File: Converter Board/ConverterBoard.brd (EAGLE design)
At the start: 101.6 x 101.3 mm, 43 parts

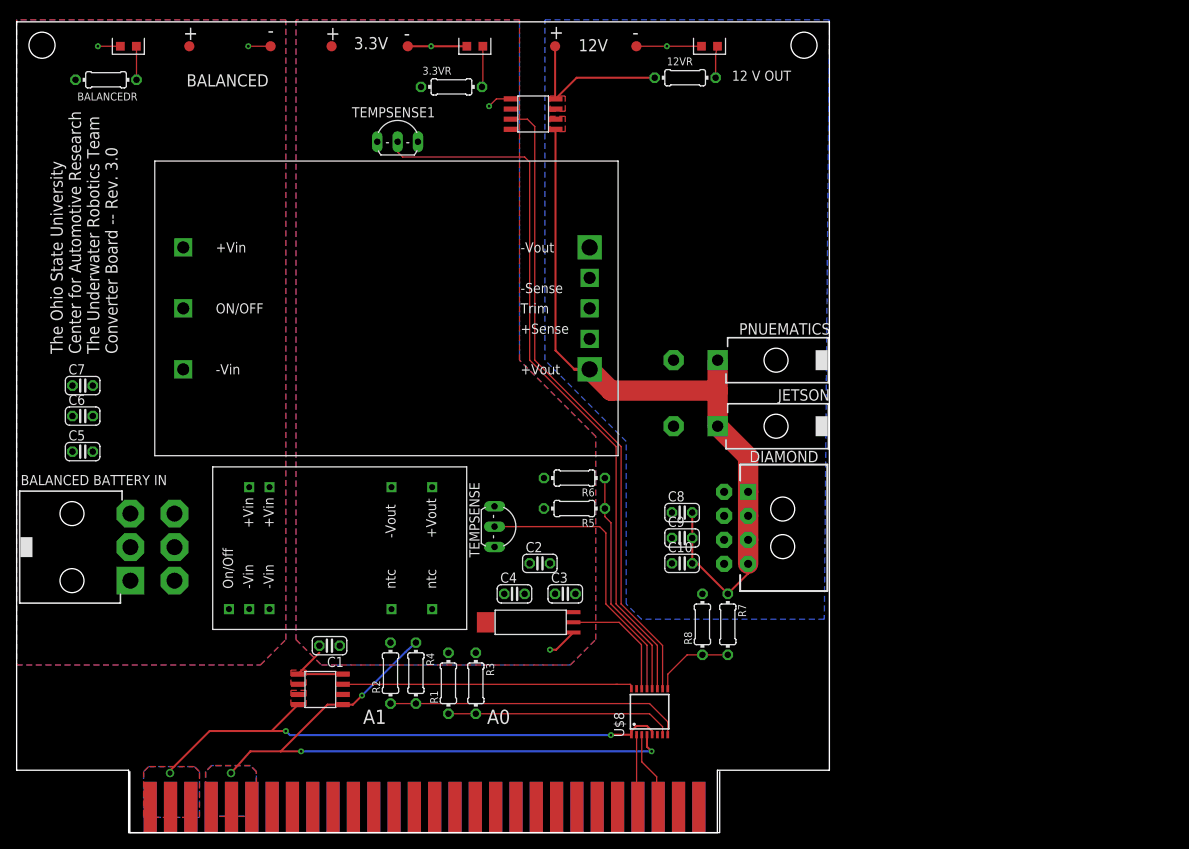
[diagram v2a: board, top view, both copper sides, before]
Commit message: Added correct capacitors, rearranged parts
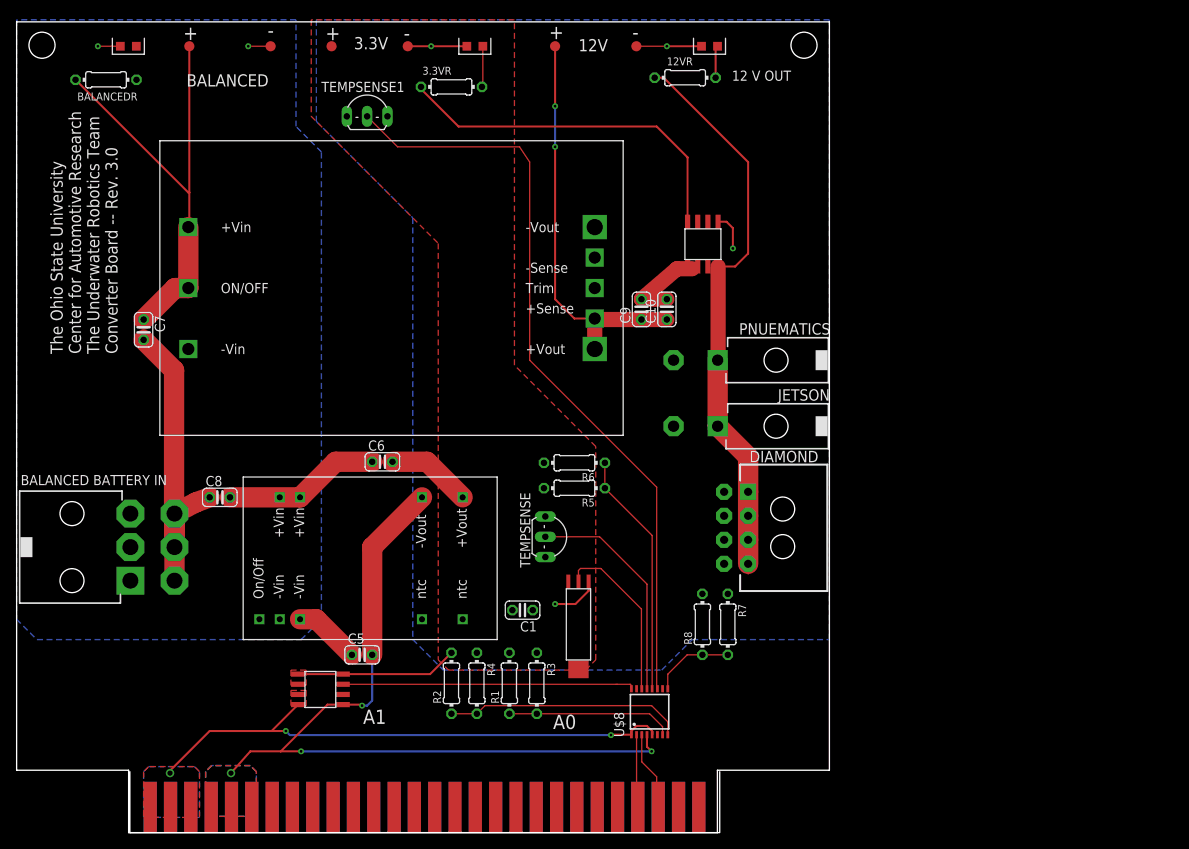
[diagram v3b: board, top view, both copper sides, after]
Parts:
- removed C2, C3, C4: (no value), resistor:C025-024X044
- C10, C8: value (none) -> 1uF
- C5, C6: value (none) -> 1000pF
- C7: value (none) -> 220uF
- C9: value (none) -> 10uF
- moved C8 57.8 mm to (25.4, 41.9)
- moved C5 43.2 mm to (43.2, 22.2)
- moved C6 37.9 mm to (45.7, 46.4)
- moved C10 31.8 mm to (81.3, 65.4), turned to 90 degrees
- moved C9 29.0 mm to (78.1, 65.4), turned to 90 degrees
- moved C1 24.5 mm to (63.2, 27.8)
- moved 12VCURRENT 23.8 mm to (83.9, 70.8), turned to 0 degrees
- moved C7 10.3 mm to (15.9, 62.9), turned to 270 degrees
- moved R2 7.73 mm to (54.4, 18.7)
- moved R4 7.73 mm to (57.5, 18.7)
- moved R1 7.62 mm to (61.6, 18.7)
- moved R3 7.62 mm to (65.0, 18.7)
- moved U$6 6.63 mm to (71.5, 31.4), turned to 180 degrees
- moved TEMPSENSE 6.48 mm to (66.1, 37.0)
- moved TEMPSENSE1 4.96 mm to (43.8, 89.5)
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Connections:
- removed net 12VGND: 12V-TP.TP, 12VCONVERTER.4,-VOUT, 12VLED.CATHODE, C10.1, C8.1, C9.1, DIAMOND.5, DIAMOND.6, DIAMOND.7, DIAMOND.8, JETSON.2, PNUEMATICS.2, R8.2
- removed net 12VMON: 12V+TP.TP, 12VCURRENT.3,IP-, 12VCURRENT.4,IP-, 12VR.1
- removed net 12VUNMON: 12VCONVERTER.8,+VOUT, 12VCURRENT.1,IP+, 12VCURRENT.2,IP+, C10.2, C8.2, C9.2, DIAMOND.1, DIAMOND.2, DIAMOND.3, DIAMOND.4, JETSON.1, PNUEMATICS.1, R7.1
- new net 12V+: 12V+TP.TP, 12VCONVERTER.7,+SENSE, 12VCONVERTER.8,+VOUT, C10.1, C9.1
- new net 12VCIN: 12VCONVERTER.1,+VIN, 12VCONVERTER.2,ON/OFF, 12VCURRENT.1,IP+, 12VCURRENT.2,IP+, BALANCED+TP.TP, BALANCEDR.2, C10.2, C7.1, C9.2, R7.1
- new net 12VCOUT: 12VCURRENT.3,IP-, 12VCURRENT.4,IP-, 12VR.1, DIAMOND.1, DIAMOND.2, DIAMOND.3, DIAMOND.4, JETSON.1, PNUEMATICS.1
- new net 3.3VC: C6.1, C8.2, U$2.22, U$2.23
- new net GND: 12V-TP.TP, 12VCONVERTER.4,-VOUT, 12VCONVERTER.5,-SENSE, 12VCURRENT.5,GND, 12VLED.CATHODE, 3.3V-TP.TP, 3.3VCURRENT.5,GND, 3.3VLED.CATHODE, C1.1, C5.2, DIAMOND.5, DIAMOND.6, DIAMOND.7, DIAMOND.8, JETSON.2, PNUEMATICS.2, R3.1, R4.1, R5.2, R8.2, TEMPSENSE.B, TEMPSENSE1.B, U$2.16, U$6.-VE, U$8.GND
- net 3.3V+: now also C6.2; no longer C2.2, C3.2, C4.2
- net 3.3VGND: no longer 12VCURRENT.5,GND, 3.3V-TP.TP, 3.3VCURRENT.5,GND, 3.3VLED.CATHODE, C1.1, C2.1, C3.1, C4.1, R3.1, R4.1, R5.2, TEMPSENSE.B, TEMPSENSE1.B, U$2.16, U$6.-VE, U$8.GND
- net BALANCED+: now also C8.1; no longer 12VCONVERTER.1,+VIN, 12VCONVERTER.2,ON/OFF, BALANCED+TP.TP, BALANCEDR.2, C5.2, C6.2, U$2.22, U$2.23
- net BALANCEDGND: no longer C6.1, C7.1
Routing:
- net GND: track 0.00 -> 125.0 mm, vias 0 -> 8
- net 12VUNMON: track 94.2 -> 0.00 mm
- net 3.3VGND: track 93.4 -> 0.00 mm, vias 7 -> 0
- net 12IDATA: track 80.3 -> 0.00 mm
- net 12VCOUT: track 0.00 -> 72.0 mm
- net 12VCIN: track 0.00 -> 68.5 mm
- net 3.3V+: track 9.37 -> 76.1 mm
- net 12V+: track 0.00 -> 50.5 mm, vias 0 -> 2
- net BALANCED+: track 0.00 -> 40.7 mm
- net 12VMON: track 20.1 -> 0.00 mm
- net 3.3VC: track 0.00 -> 19.6 mm
- net BALANCEDGND: track 5.60 -> 13.9 mm
- net 12VGND: track 8.14 -> 0.00 mm, vias 1 -> 0
- net TEMPDATA: track 35.8 -> 28.2 mm
- net A0: track 28.4 -> 20.8 mm
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- added copper zone on layer 16, net GND
- removed copper zone on layer 16, net 12VGND
- removed copper zone on layer 1, net 12VMON
- removed copper zone on layer 1, net 12VUNMON
- removed copper zone on layer 1, net BALANCED+

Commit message: Finished Rev 3 of converter board
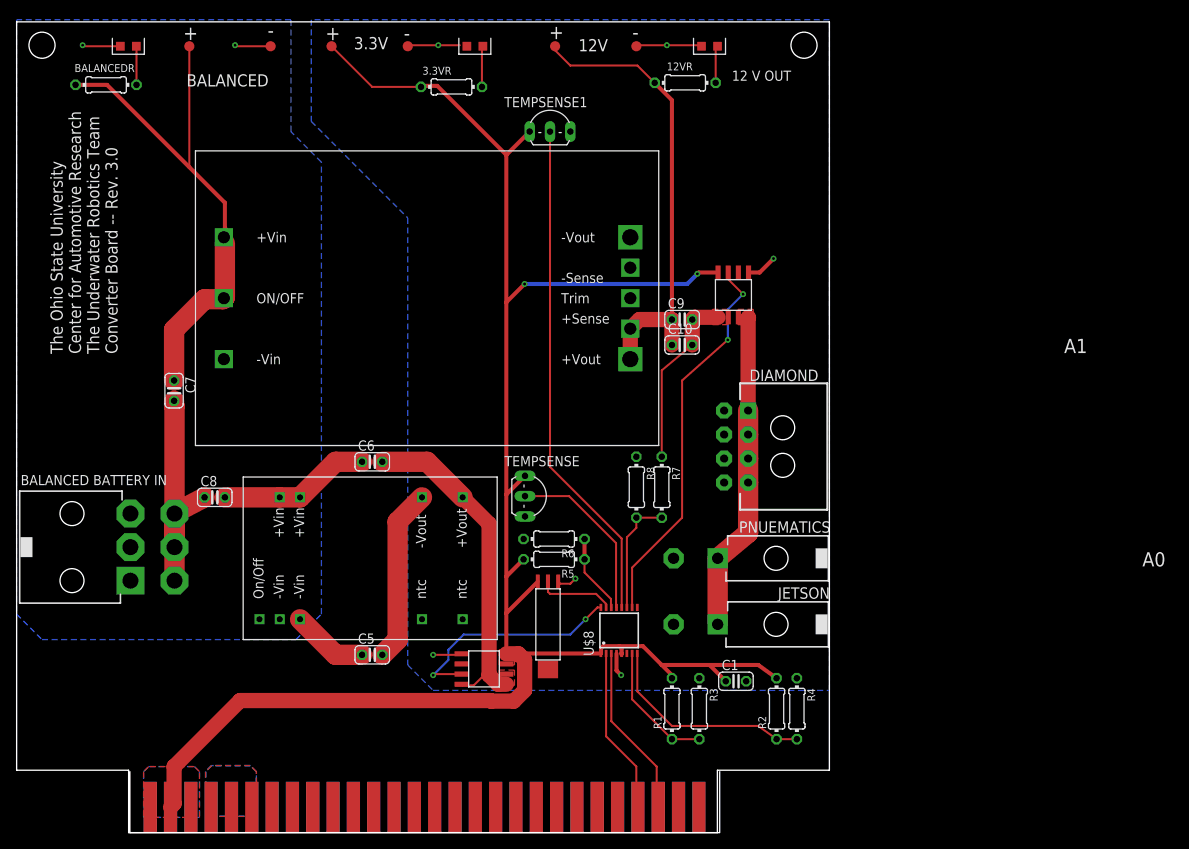
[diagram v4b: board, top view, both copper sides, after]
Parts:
- moved R2 40.8 mm to (95.0, 15.5)
- moved R4 40.1 mm to (97.5, 15.5)
- moved C1 28.1 mm to (89.9, 18.9), turned to 0 degrees
- moved 3.3VCURRENT 26.1 mm to (61.2, 18.5), turned to 90 degrees
- moved PNUEMATICS 24.8 mm to (87.6, 34.3)
- moved JETSON 24.8 mm to (87.6, 26.0)
- moved TEMPSENSE1 22.9 mm to (66.7, 87.6)
- moved R1 20.6 mm to (81.9, 15.5)
- moved R3 20.6 mm to (85.3, 15.5)
- moved R7 19.0 mm to (80.6, 43.2)
- moved R8 19.0 mm to (77.5, 43.2), turned to 270 degrees
- moved U$8 10.9 mm to (75.3, 25.3)
- moved DIAMOND 10.2 mm to (91.4, 48.3)
- moved R6 9.86 mm to (67.2, 36.7)
- moved R5 9.25 mm to (67.2, 34.2)
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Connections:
- net 12IDATA renamed 12VCURRENTDATA
- net 3.3IDATA renamed 3.3VCURRENTDATA
- net 3.3VC renamed 3.3VCONVIN
- removed net 12V+: 12V+TP.TP, 12VCONVERTER.7,+SENSE, 12VCONVERTER.8,+VOUT, C10.1, C9.1
- removed net 12VCIN: 12VCONVERTER.1,+VIN, 12VCONVERTER.2,ON/OFF, 12VCURRENT.1,IP+, 12VCURRENT.2,IP+, BALANCED+TP.TP, BALANCEDR.2, C10.2, C7.1, C9.2, R7.1
- removed net 12VCOUT: 12VCURRENT.3,IP-, 12VCURRENT.4,IP-, 12VR.1, DIAMOND.1, DIAMOND.2, DIAMOND.3, DIAMOND.4, JETSON.1, PNUEMATICS.1
- removed net 12VDATA: R7.2, R8.1, U$8.IN7
- removed net 3.3V+: 12VCURRENT.8,VCC, 3.3V+TP.TP, 3.3VCURRENT.1,IP+, 3.3VCURRENT.2,IP+, 3.3VCURRENT.8,VCC, 3.3VR.2, C1.2, C6.2, R1.2, R2.2, R6.2, TEMPSENSE.E, TEMPSENSE1.E, U$2.14, U$6.+VE
- removed net GND: 12V-TP.TP, 12VCONVERTER.4,-VOUT, 12VCONVERTER.5,-SENSE, 12VCURRENT.5,GND, 12VLED.CATHODE, 3.3V-TP.TP, 3.3VCURRENT.5,GND, 3.3VLED.CATHODE, C1.1, C5.2, DIAMOND.5, DIAMOND.6, DIAMOND.7, DIAMOND.8, JETSON.2, PNUEMATICS.2, R3.1, R4.1, R5.2, R8.2, TEMPSENSE.B, TEMPSENSE1.B, U$2.16, U$6.-VE, U$8.GND
- removed net VCC: 3.3VCURRENT.3,IP-, 3.3VCURRENT.4,IP-, U$3.3.3VP1, U$3.3.3VP2, U$3.3.3VP3, U$3.3.3V_4, U$3.3.3V_5, U$3.3.3V_6, U$8.V+, U$8.VREF
- new net 12VCONV+: 12V+TP.TP, 12VCONVERTER.7,+SENSE, 12VCONVERTER.8,+VOUT, 12VR.1, C10.1, C9.1
- new net 12VCONVIN: 12VCONVERTER.1,+VIN, 12VCONVERTER.2,ON/OFF, BALANCED+TP.TP, BALANCEDR.1, C7.1
- new net 12VCURRENTIN: 12VCURRENT.1,IP+, 12VCURRENT.2,IP+, C10.2, C9.2, R7.1
- new net 12VCURRENTOUT: 12VCURRENT.3,IP-, 12VCURRENT.4,IP-, DIAMOND.1, DIAMOND.2, DIAMOND.3, DIAMOND.4, JETSON.1, PNUEMATICS.1
- new net 12VDIV: R7.2, R8.2, U$8.IN5
- new net 3.3VCONVOUT: 3.3VCURRENT.1,IP+, 3.3VCURRENT.2,IP+, 3.3VCURRENT.8,VCC, C6.2, U$2.14
- new net 3.3VCURRENTOUT: 12VCURRENT.8,VCC, 3.3V+TP.TP, 3.3VCURRENT.3,IP-, 3.3VCURRENT.4,IP-, 3.3VR.2, C1.1, R1.2, R2.2, R5.2, TEMPSENSE.E, TEMPSENSE1.E, U$3.3.3VP1, U$3.3.3VP2, U$3.3.3VP3, U$3.3.3V_4, U$3.3.3V_5, U$3.3.3V_6, U$6.+VE, U$8.V+, U$8.VREF
- new net CMGND: 12V-TP.TP, 12VCONVERTER.4,-VOUT, 12VCONVERTER.5,-SENSE, 12VCURRENT.5,GND, 12VLED.CATHODE, 3.3V-TP.TP, 3.3VCURRENT.5,GND, 3.3VLED.CATHODE, C1.2, C5.2, DIAMOND.5, DIAMOND.6, DIAMOND.7, DIAMOND.8, JETSON.2, PNUEMATICS.2, R3.1, R4.1, R6.2, R8.1, TEMPSENSE.B, TEMPSENSE1.B, U$2.16, U$6.-VE, U$8.GND
- net 3.3VDATA: now also U$8.IN2; no longer U$8.IN4
- net BALANCEDGND: no longer U$2.1
- net BALANCEDLED: now also BALANCEDR.2; no longer BALANCEDR.1
- net HUMIDITYDATA: now also U$8.IN1; no longer U$8.IN2
- net TEMP1DATA: now also U$8.IN4; no longer U$8.IN5
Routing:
- net 3.3VCURRENTOUT: track 0.00 -> 234.0 mm, vias 0 -> 2
- net GND: track 125.0 -> 0.00 mm, vias 8 -> 0
- net 3.3V+: track 76.1 -> 0.00 mm
- net 12VCOUT: track 72.0 -> 0.00 mm
- net VCC: track 69.0 -> 0.00 mm, vias 3 -> 0
- net 12VCIN: track 68.5 -> 0.00 mm
- net 12VCONVIN: track 0.00 -> 66.0 mm
- net 12VCONV+: track 0.00 -> 57.8 mm
- net CMGND: track 0.00 -> 51.2 mm, vias 0 -> 6
- net 12V+: track 50.5 -> 0.00 mm, vias 2 -> 0
- net 12VCURRENTDATA: track 0.00 -> 48.6 mm, vias 0 -> 2
- net 3.3VCONVOUT: track 0.00 -> 42.1 mm
- net 12VCURRENTOUT: track 0.00 -> 40.2 mm
- net TEMP1DATA: track 95.4 -> 63.2 mm
- net 12VCURRENTIN: track 0.00 -> 22.3 mm
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- added copper zone on layer 1, net 12VCURRENTIN
- added copper zone on layer 1, net 12VCURRENTOUT
- added copper zone on layer 1, net 3.3VCONVOUT
- added copper zone on layer 1, net 3.3VCURRENTOUT
- added copper zone on layer 16, net CMGND
- removed copper zone on layer 1, net 3.3V+
- removed copper zone on layer 1, net 3.3VBKPLN
- removed copper zone on layer 16, net GND

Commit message: Finished rev3 of board, made gerber files
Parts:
- removed C1: 0.1 uF, resistor:C025-024X044
- removed C10, C8: 1uF, resistor:C025-024X044
- removed C6: 1000pF, resistor:C025-024X044
- removed C7: 220uF, resistor:C025-024X044
- removed C9: 10uF, resistor:C025-024X044
- added C11, C14: 1uF, capacitor-wima:C5B3
- added C12: 220uF, capacitor-wima:C5B3
- added C13: 10uF, capacitor-wima:C5B3
- added C3, C4: 1000pF, capacitor-wima:C5B3
- added SCL, SDA: TPPAD1-20, testpad:P1-20
- C5: value 1000pF -> 0.1uF; device resistor:C025-024X044 -> capacitor-wima:C2.5-2
- moved C5 46.5 mm to (90.8, 19.1), turned to 180 degrees
- moved 12VCURRENT 3.17 mm to (90.9, 64.4)
- moved R1 1.27 mm to (83.2, 15.5)
- moved R2 0.64 mm to (95.6, 15.5)
- moved R3 0.64 mm to (86.0, 15.5)
- moved R4 0.64 mm to (98.2, 15.5)
- renumbered U$8 to ADC
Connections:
- removed net 3.3VGND: U$3.GND1, U$3.GND2, U$3.GND3, U$3.GND_4, U$3.GND_5, U$3.GND_6
- net 12VCONV+: now also C13.1, C14.1; no longer C10.1, C9.1
- net 12VCONVIN: now also C12.2; no longer C7.1
- net 12VCURRENTIN: now also C13.2, C14.2; no longer C10.2, C9.2
- net 3.3VCONVIN: now also C11.2, C3.1; no longer C6.1, C8.2
- net 3.3VCONVOUT: now also C3.2; no longer C6.2
- net 3.3VCURRENTOUT: now also C5.2; no longer C1.1
- net BALANCED+: now also C11.1, C12.1; no longer C7.2, C8.1
- net BALANCEDGND: now also C4.1; no longer C5.1
- net CMGND: now also C4.2, C5.1, U$3.GND1, U$3.GND2, U$3.GND3, U$3.GND_4, U$3.GND_5, U$3.GND_6; no longer C1.2, C5.2
- net SCL: now also SCL.TP
- net SDA: now also SDA.TP
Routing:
- net CMGND: track 51.2 -> 79.5 mm, vias 6 -> 7
- net 3.3VCURRENTOUT: track 234.0 -> 250.9 mm, vias 2 -> 3
- net 12VCURRENTIN: track 22.3 -> 29.7 mm
- net SDA: track 20.2 -> 26.8 mm
- net BALANCED+: track 31.0 -> 35.9 mm
- net 12VCONVIN: track 66.0 -> 61.6 mm
- net SCL: track 21.7 -> 25.2 mm
- net 3.3VCURRENTDATA: track 28.8 -> 32.3 mm
- net 12VCURRENTOUT: track 40.2 -> 42.8 mm
- net 12VCONV+: track 57.8 -> 55.4 mm
- net 3.3VCONVOUT: track 42.1 -> 40.3 mm
- net BALANCEDGND: track 18.9 -> 17.8 mm
- net A1: track 27.0 -> 27.6 mm
- net A0: track 16.2 -> 16.8 mm
- net 12VCURRENTDATA: track 48.6 -> 49.2 mm
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- added copper zone on layer 16, net 3.3VCURRENTOUT
- added copper zone on layer 1, net CMGND
- removed copper zone on layer 1, net 12VCURRENTIN
- removed copper zone on layer 1, net 12VCURRENTOUT
- removed copper zone on layer 1, net 3.3VGND
- removed copper zone on layer 16, net 3.3VGND
- removed copper zone on layer 1, net VCC
- removed copper zone on layer 16, net VCC

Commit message: Revamped Converter Board
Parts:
- added 12V, 3.3V: 39-30-02?, con-molex-mini-fit:39-30-?02?
- moved 12VCURRENT 13.7 mm to (90.9, 78.1)
- moved C12 8.76 mm to (17.1, 66.8), turned to 180 degrees
- moved DIAMOND 8.64 mm to (91.4, 56.9)
- moved C4 6.38 mm to (38.1, 21.0)
- moved C13 4.57 mm to (85.1, 68.7)
- moved C14 4.32 mm to (85.1, 72.3)
- moved R7 4.20 mm to (76.8, 45.0)
- moved R8 4.20 mm to (73.7, 45.0)
- moved C11 3.44 mm to (25.1, 34.0)
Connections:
- removed net 12VCONVIN: 12VCONVERTER.1,+VIN, 12VCONVERTER.2,ON/OFF, BALANCED+TP.TP, BALANCEDR.1, C12.2
- removed net 12VCURRENTIN: 12VCURRENT.1,IP+, 12VCURRENT.2,IP+, C13.2, C14.2, R7.1
- net 12VCONV+: now also 12VCURRENT.1,IP+, 12VCURRENT.2,IP+, R7.1
- net 12VCURRENTOUT: now also 12V.1
- net 3.3VCURRENTOUT: now also 3.3V.1
- net BALANCED+: now also 12VCONVERTER.1,+VIN, 12VCONVERTER.2,ON/OFF, BALANCED+TP.TP, BALANCEDR.1
- net BALANCEDGND: now also C12.2
- net CMGND: now also 12V.2, 3.3V.2, C13.2, C14.2
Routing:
- net BALANCED+: track 35.9 -> 104.8 mm
- net 12VCONVIN: track 61.6 -> 0.00 mm
- net 12VCURRENTIN: track 29.7 -> 0.00 mm
- net 12VCURRENTOUT: track 42.8 -> 61.0 mm
- net 12VCONV+: track 55.4 -> 71.6 mm, vias 0 -> 2
- net 12VCURRENTDATA: track 49.2 -> 62.2 mm
- net 3.3VCURRENTOUT: track 250.9 -> 257.4 mm, vias 3 -> 2
- net BALANCEDGND: track 17.8 -> 15.0 mm
- net 12VDIV: track 14.9 -> 17.3 mm
- net 3.3VCONVIN: track 19.5 -> 20.9 mm
- net 3.3VCONVOUT: track 40.3 -> 41.3 mm
- added copper zone on layer 1, net 12VCONV+
- added copper zone on layer 1, net 12VCURRENTOUT
